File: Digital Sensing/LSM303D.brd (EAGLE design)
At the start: 7 parts

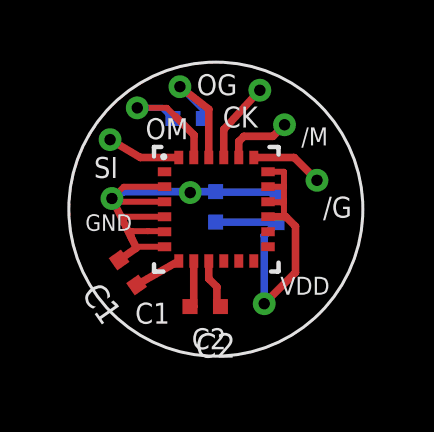
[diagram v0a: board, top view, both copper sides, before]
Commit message: minor modification on OSHW logo; added LSM330DLC reference design
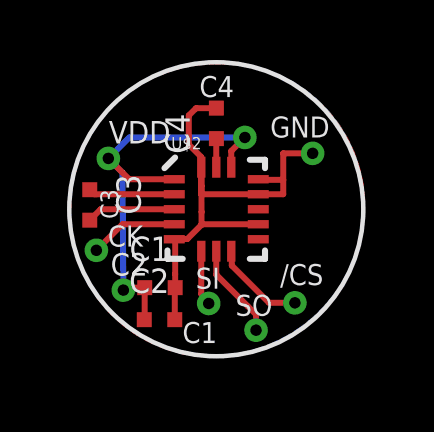
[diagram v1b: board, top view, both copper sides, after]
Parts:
- removed R1: (no value), rc-master-smd:R0402
- removed U$1: LSM9DS09DOFS0, lsm9ds0:LGA24(4X4X1)
- added U$2: LSM303D, SparkFun-Sensors:LGA16-3MM
- C1: value 4.7uF -> 10u
- C2: value 0.22uF -> 100n
- C3: value 10uF -> 220n
- C4: value 100nF -> 10n
- moved C3 4.20 mm to (-4.22, 0.14), flipped to the top
- moved C4 3.46 mm to (0.00, 2.86), flipped to the top, turned to 90 degrees
- moved C2 1.58 mm to (-1.89, -3.68), turned to 0 degrees
- moved C1 1.18 mm to (-1.88, -2.61), turned to 0 degrees
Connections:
- removed net CS_G: U$1.P$19
- removed net CS_XM: U$1.P$20
- removed net N$1: C1.1, U$1.P$7
- removed net N$3: C2.1, U$1.P$9
- removed net SDO_G: R1.1, U$1.P$22
- removed net SDO_XM: R1.2, U$1.P$23
- new net /CS: U$2.8
- new net N$10: C4.1, U$2.15
- new net N$11: C3.2, U$2.3
- new net SDO: U$2.7
- net GND: now also C2.2, C4.2, U$2.10, U$2.12, U$2.13, U$2.16, U$2.5; no longer C3.1, C4.1, U$1.P$2, U$1.P$3, U$1.P$4, U$1.P$5, U$1.P$6
- net N$2: now also C3.1, U$2.2; no longer C2.2, U$1.P$8
- net SDI: now also U$2.6; no longer U$1.P$24
- net SPC: now also U$2.4; no longer U$1.P$21
- net VDD: now also C1.1, C2.1, U$2.1, U$2.14; no longer C3.2, C4.2, U$1.P$15, U$1.P$16, U$1.P$17, U$1.P$18
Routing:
- net SDO_XM: track 4.36 -> 0.00 mm, vias 1 -> 0
- net SDO_G: track 4.21 -> 0.00 mm, vias 1 -> 0
- net SDO: track 0.00 -> 3.18 mm, vias 0 -> 1
- net /CS: track 0.00 -> 3.10 mm, vias 0 -> 1
- net N$11: track 0.00 -> 2.97 mm
- net CS_G: track 2.42 -> 0.00 mm, vias 1 -> 0
- net CS_XM: track 2.29 -> 0.00 mm, vias 1 -> 0
- net N$3: track 1.75 -> 0.00 mm
- net VDD: track 13.2 -> 14.9 mm, vias 1 -> 3
- net GND: track 15.7 -> 17.4 mm, vias 2 -> 1
- net N$1: track 1.62 -> 0.00 mm
- net N$2: track 1.65 -> 2.88 mm
- net N$10: track 0.00 -> 0.96 mm
- net SDI: track 2.45 -> 1.83 mm
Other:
- board text added: "/CS"
- board text added: "LSM303D"
- board text added: "SO"
- board text removed: "/G"
- board text removed: "/M"
- board text removed: "LSM9DS0"
- board text removed: "OG"
- board text removed: "OM"
- board text removed: "R1"
